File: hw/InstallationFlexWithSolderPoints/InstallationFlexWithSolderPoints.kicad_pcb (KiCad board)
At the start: 2 copper layers, 84.4 x 60.5 mm, 24 parts, among them J1 +5V, J10 D4, J11 BRIGHT, J15 GND, J16 GND, J17 Conn_01x16, J2 GND, J3 CLK, J4 SMS, J5 DW, J6 CL2, J7 D1, J8 D2, J9 D3

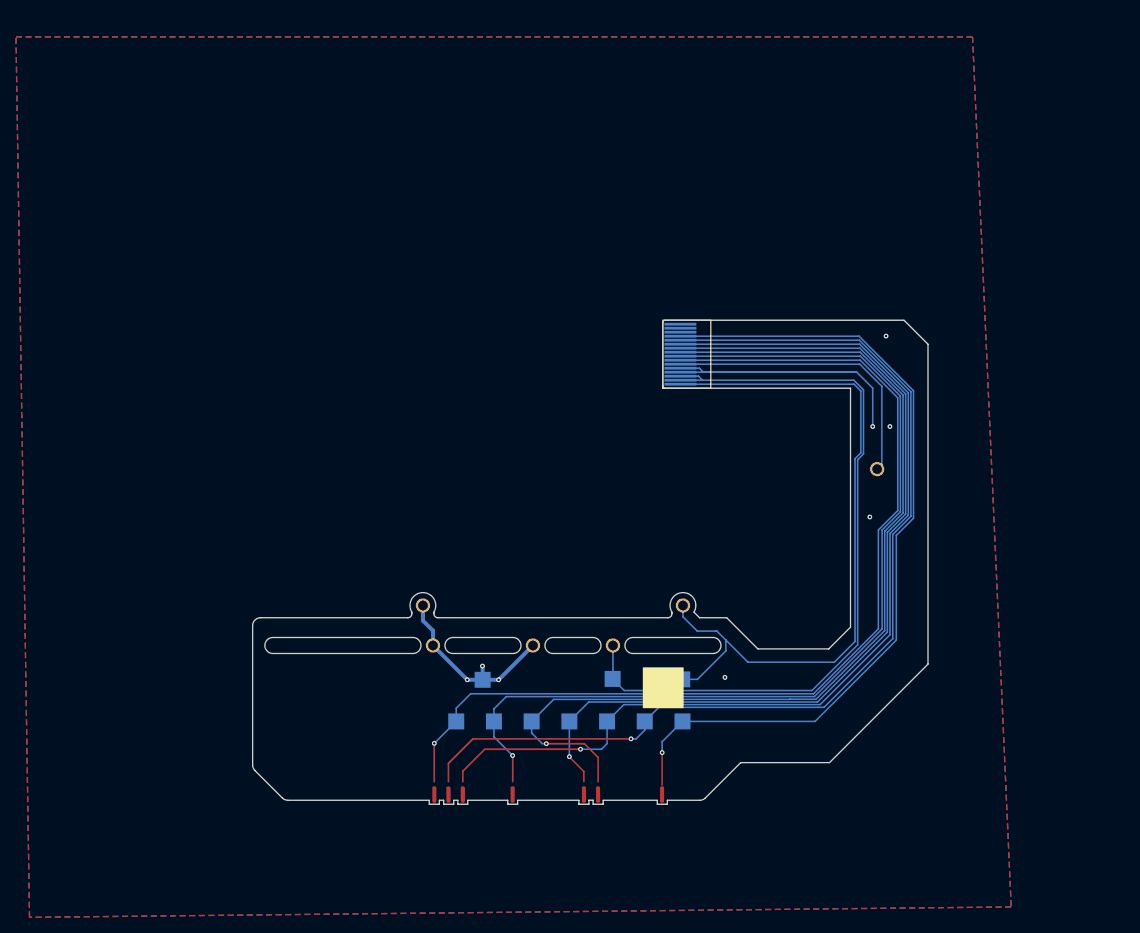
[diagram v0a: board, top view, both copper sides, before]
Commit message: Updated pin assignments on main PCB to match pico code using the correct sequential pins.
54PinTo60RibbonAdapterBoard tweaked trace layout to reduce overall board size slightly.
Added InstallationFlexWithSolderPoints for installing without a ribbon connector.
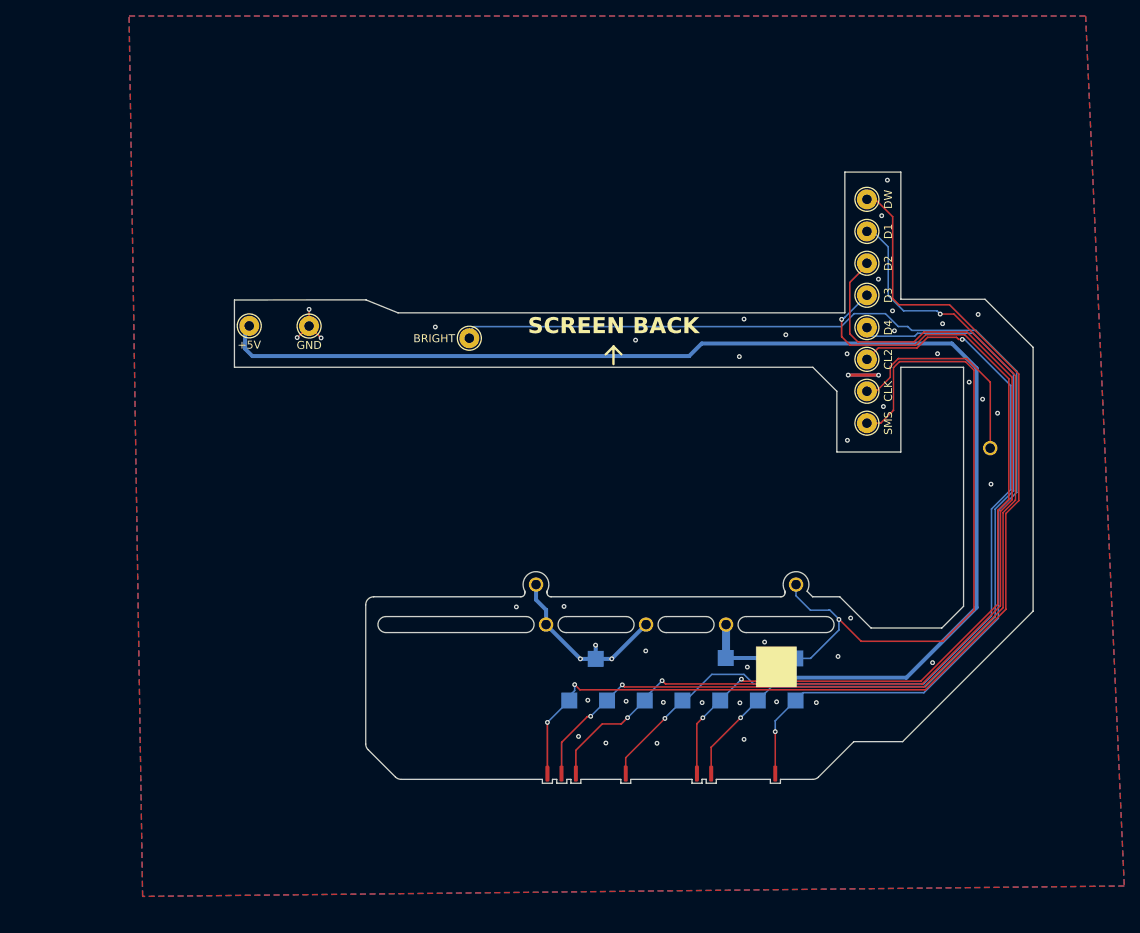
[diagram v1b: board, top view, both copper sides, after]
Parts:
- removed J17: Conn_01x16, gg_lcd:Flex Connector 0.5mm 01x16Pin
- added J18: GND, InstallationBoard:TestPoint_THTPad_D2.5mm_Drill1.2mm_Front, F.Cu at (113.0, 86.3)
- added J20: +5V, InstallationBoard:TestPoint_THTPad_D2.5mm_Drill1.2mm_Front, F.Cu at (105.5, 86.2)
- added J21: SMS, InstallationBoard:TestPoint_THTPad_D2.5mm_Drill1.2mm_Front, F.Cu at (182.8, 98.4)
- added J22: CLK, InstallationBoard:TestPoint_THTPad_D2.5mm_Drill1.2mm_Front, F.Cu at (182.8, 94.4)
- added J23: CL2, InstallationBoard:TestPoint_THTPad_D2.5mm_Drill1.2mm_Front, F.Cu at (182.8, 90.4)
- added J24: D4, InstallationBoard:TestPoint_THTPad_D2.5mm_Drill1.2mm_Front, F.Cu at (182.8, 86.5)
- added J25: D3, InstallationBoard:TestPoint_THTPad_D2.5mm_Drill1.2mm_Front, F.Cu at (182.8, 82.4)
- added J26: D2, InstallationBoard:TestPoint_THTPad_D2.5mm_Drill1.2mm_Front, F.Cu at (182.8, 78.4)
- added J27: D1, InstallationBoard:TestPoint_THTPad_D2.5mm_Drill1.2mm_Front, F.Cu at (182.8, 74.4)
- added J28: DW, InstallationBoard:TestPoint_THTPad_D2.5mm_Drill1.2mm_Front, F.Cu at (182.8, 70.4)
- added J29: BRIGHT, InstallationBoard:TestPoint_THTPad_D2.5mm_Drill1.2mm_Front, F.Cu at (133.1, 87.8)
- J10, J11, J5, J6, J7, J8, J9: footprint InstallationBoard:SolderWirePad_1x01_SMD_1x2mm -> InstallationBoard:SolderWirePad_1x01_Edge_1x2mm
- TP10: value D4 -> D1
- TP7: value D1 -> D4
- TP8: value D2 -> D3
- TP9: value D3 -> D2
- moved TP6 23.7 mm to (159.7, 133.1)
- moved TP4 14.4 mm to (173.8, 127.8)
- moved TP5 14.4 mm to (145.6, 133.1)
- moved TP7 14.4 mm to (169.1, 133.1)
- moved J10 14.4 mm to (163.3, 142.2)
- moved J11 14.4 mm to (171.3, 142.2)
- moved J15 14.4 mm to (141.4, 118.6)
- moved J3 14.4 mm to (198.2, 101.5)
- moved J4 14.4 mm to (173.9, 118.6)
- moved J5 14.4 mm to (142.8, 142.2)
- moved J6 14.4 mm to (152.6, 142.2)
- moved J7 14.4 mm to (144.6, 142.2)
- moved J8 14.4 mm to (146.4, 142.2)
- moved J9 14.4 mm to (161.5, 142.2)
- moved TP11 14.4 mm to (173.8, 133.1)
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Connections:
- TP10 pad 1: D4 -> D1
- TP7 pad 1: D1 -> D4
- TP8 pad 1: D2 -> D3
- TP9 pad 1: D3 -> D2
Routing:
- net +5V: track 96.3 -> 167.2 mm
- net BRIGHT: track 104.0 -> 144.9 mm
- net GND: track 75.2 -> 37.2 mm, vias 8 -> 47
- net D4: track 123.3 -> 97.7 mm
- net CL2: track 122.3 -> 107.5 mm, vias 1 -> 2
- net DW: track 126.2 -> 135.1 mm, vias 1 -> 2
- net CLK: track 36.9 -> 28.7 mm
- net D3: track 113.9 -> 109.6 mm, vias 1 -> 3
- net D1: track 128.2 -> 125.2 mm, vias 1 -> 3
- net SMS: track 89.1 -> 86.5 mm, vias 0 -> 1
- net D2: track 125.6 -> 126.2 mm, vias 1 -> 2
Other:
- board size 84.4 x 60.5 mm -> 99.8 x 76.4 mm
- board text added: "SCREEN BACK"
- board text added: "SCREEN FRONT"
- board text removed: "THIS SIDE UP"

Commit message: Increased text size on installation flex
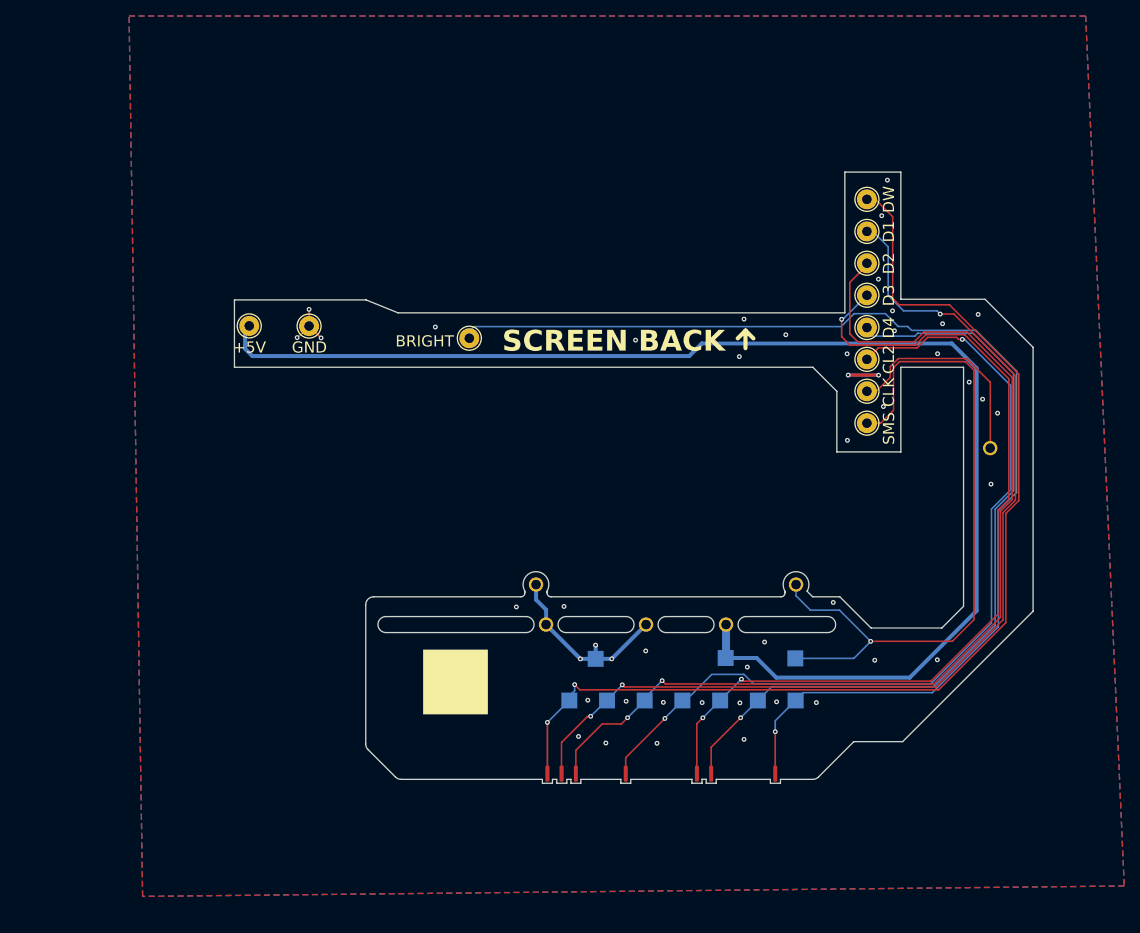
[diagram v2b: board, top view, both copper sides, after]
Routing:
- net SMS: track 86.5 -> 89.3 mm
- net DW: track 135.1 -> 136.1 mm
- net D1: track 125.2 -> 126.1 mm
- net D2: track 126.2 -> 127.1 mm
- net D3: track 109.6 -> 110.3 mm
- net BRIGHT: track 144.9 -> 145.5 mm
- net D4: track 97.7 -> 98.3 mm
- net CL2: track 107.5 -> 108.0 mm
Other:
- outline, holes or cut-outs redrawn
